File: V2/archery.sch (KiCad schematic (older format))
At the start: 27 parts, among them J0 Molex_PSU_F, J1 Jumper_M, J2 Flat_7seg_F, J3 Flat_Rpi_Data_F, Q0 BD139-16, Q1 BD139-16, Q2 BD139-16, Q3 BD139-16, Q4 BD139-16, Q5 BD139-16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

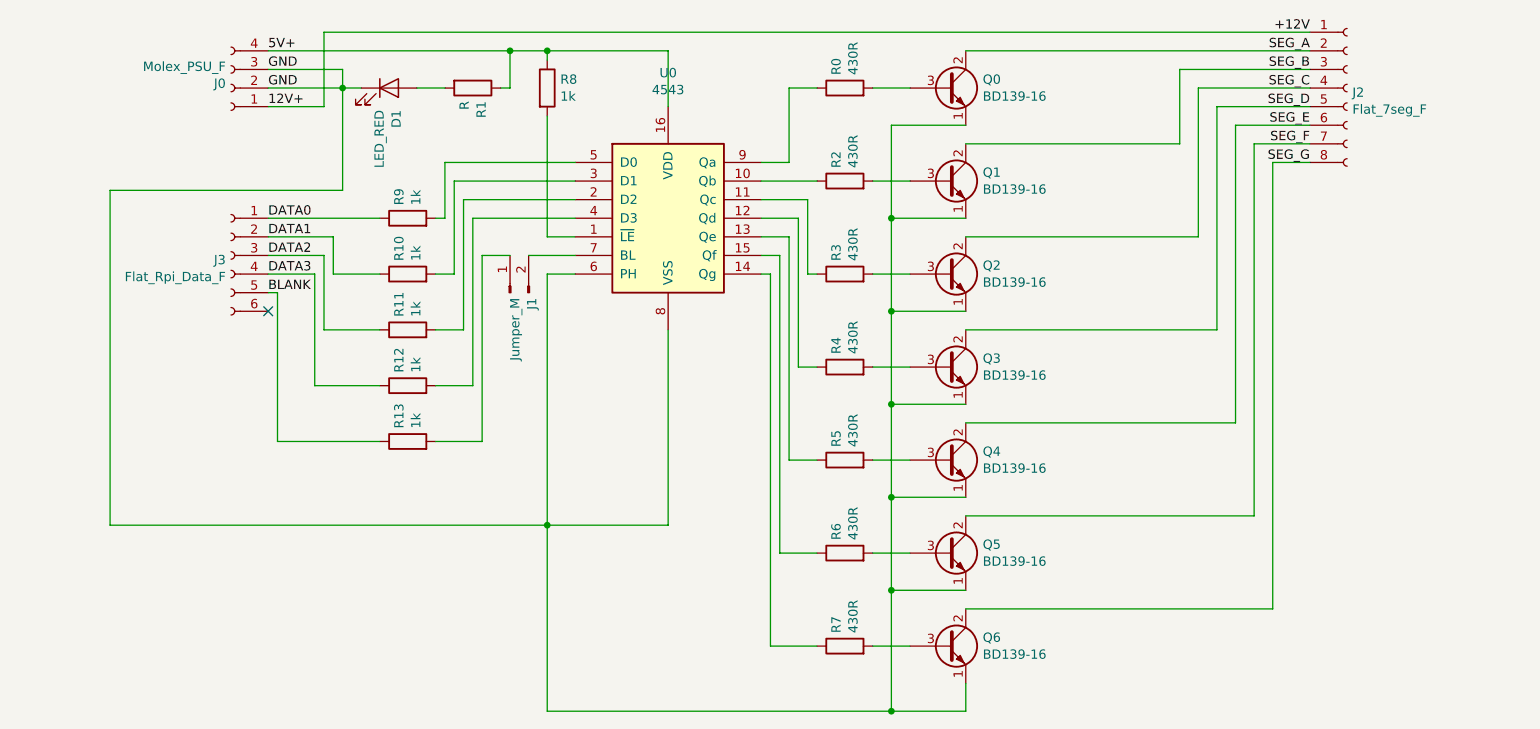
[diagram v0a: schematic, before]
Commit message: Switch driver IC
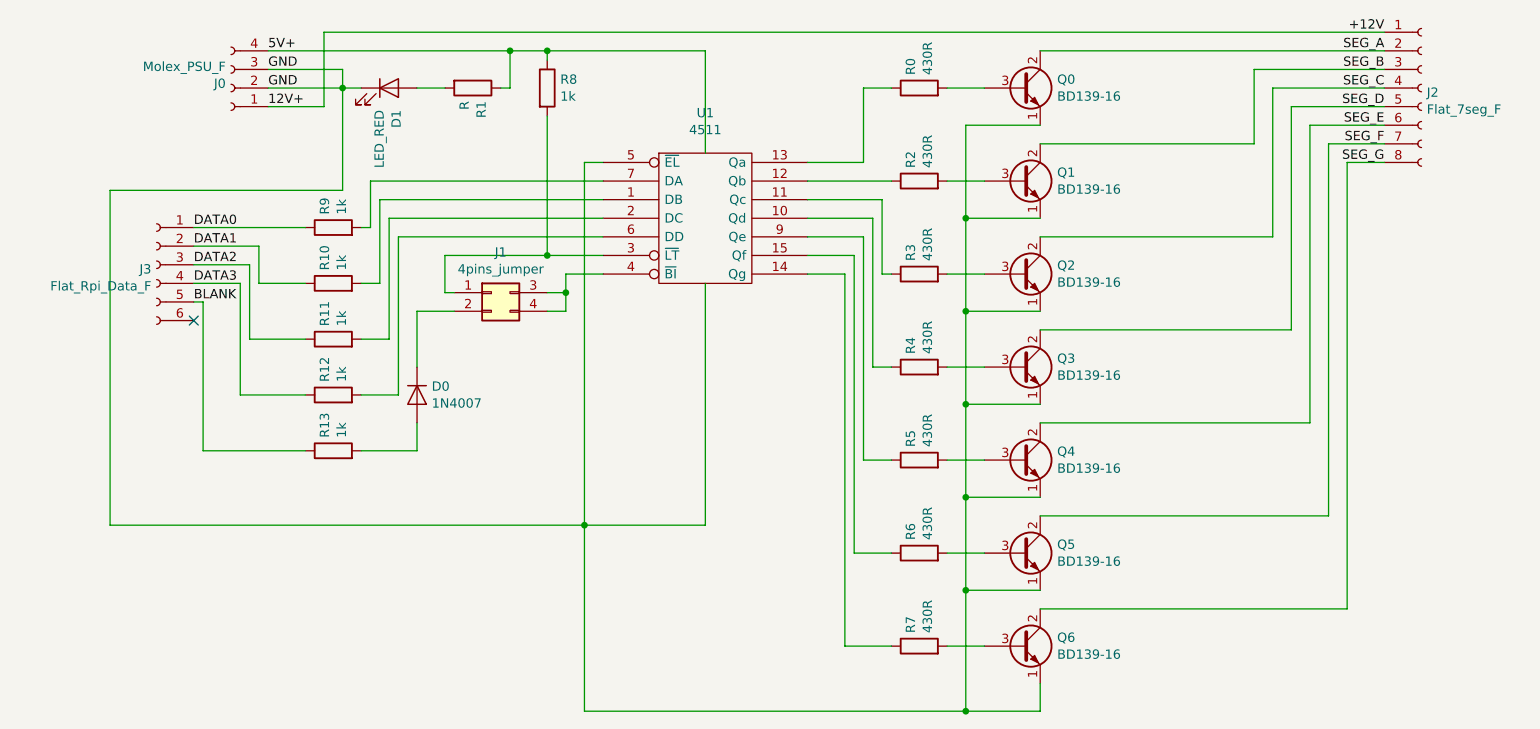
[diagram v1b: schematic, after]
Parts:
- removed J1: Jumper_M, symbol Connector:Conn_01x02_Male
- removed U0: 4543, symbol 4xxx:4543
- added D0: 1N4007, symbol Device:D
- added J1: 4pins_jumper, symbol Connector_Generic:Conn_02x02_Top_Bottom
- added U1: 4511, symbol 4xxx_IEEE:4511
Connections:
- net at R8.2: now also J1.1 (Pin_1), U1.3 (~LT)
- net at R2.1: now also U1.12 (Qb)
- net at R3.1: now also U1.11 (Qc)
- net at R4.1: now also U1.10 (Qd)
- net at R5.1: now also U1.9 (Qe)
- net at R7.1: now also U1.14 (Qg)
- net at R6.1: now also U1.15 (Qf)
- net at R11.2: now also U1.2 (DC)
- net at R10.2: now also U1.1 (DB)
- net at R12.2: now also U1.6 (DD)
- net at R9.2: now also U1.7 (DA)
- net at R0.1: now also U1.13 (Qa)
- net at R13.2: now also D0.2 (A)
- net 5V+ renamed Vdd
- net Vdd: now also U1.16 (Vdd)
- net GND renamed Vss
- net Vss: now also U1.5 (~EL), U1.8 (Vss)
- new net: J1.3 (Pin_3), J1.4 (Pin_4), U1.4 (~BI)
- new net: D0.1 (K), J1.2 (Pin_2)
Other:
- moved on the sheet: J2, J3, Q0, Q1, Q2, Q3, Q4, Q5, Q6, R0, R10, R11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
